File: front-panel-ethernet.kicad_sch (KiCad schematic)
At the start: 0 parts

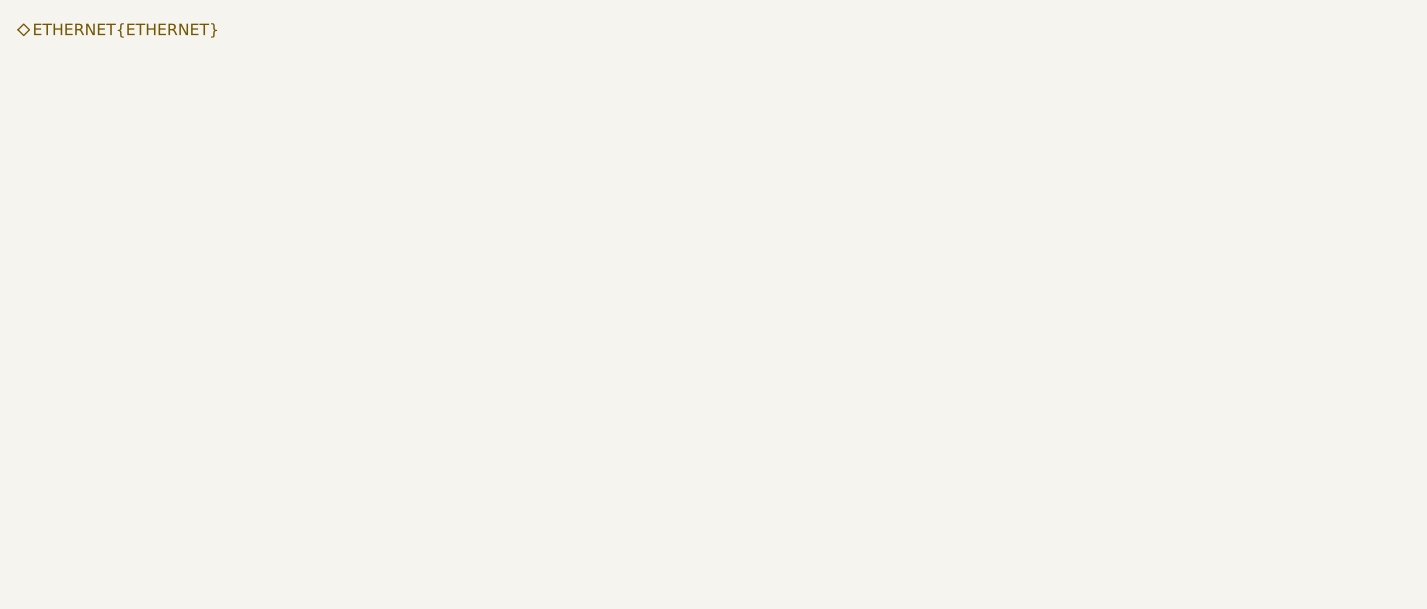
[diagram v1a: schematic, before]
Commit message: [#82153] Add RJ45 connector
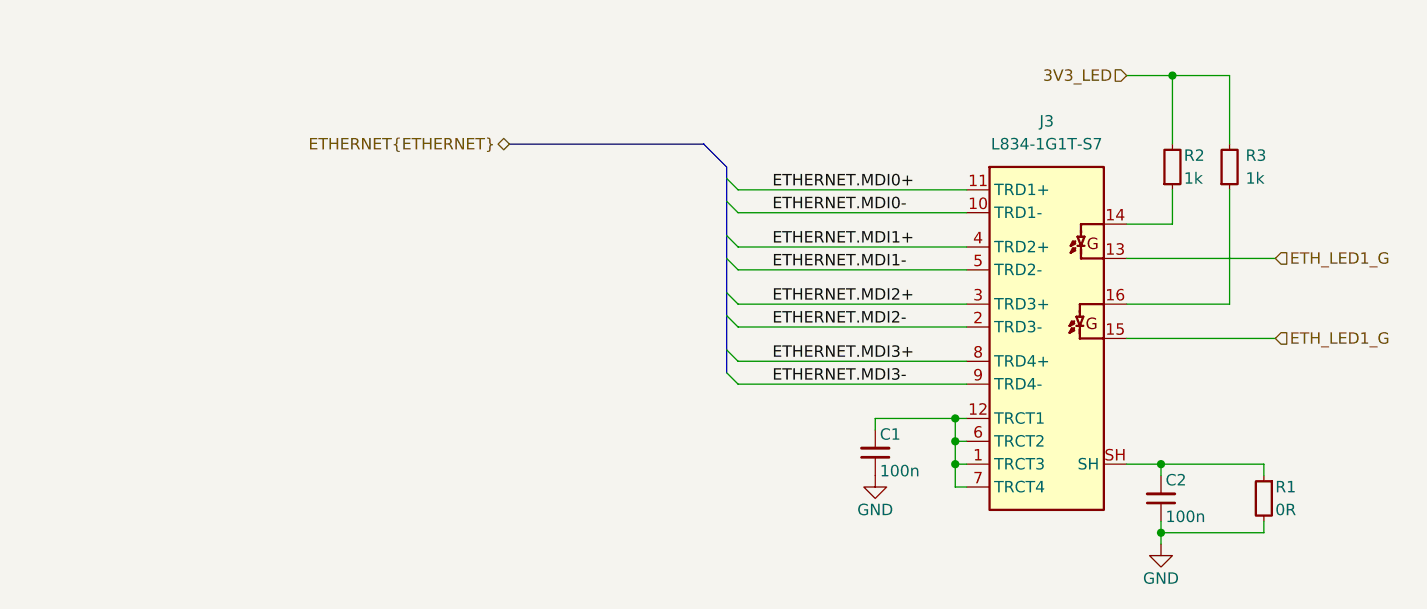
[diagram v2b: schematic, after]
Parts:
- added C1, C2: C_100n_0402, antmicro-footprints:C_0402_1005Metric, symbol antmicroCapacitors0402:C_100n_0402
- added J3: L834-1G1T-S7, antmicro-footprints:RJ45_BEL_L834-1G1T-S7, symbol antmicroModularConnectorsJacksWithMagnetics:L834-1G1T-S7
- added R1: R_0R_0402, antmicro-footprints:R_0402_1005Metric, symbol antmicroResistors0402:R_0R_0402
- added R2, R3: R_1k_0402, antmicro-footprints:R_0402_1005Metric, symbol antmicroResistors0402:R_1k_0402
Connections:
- new net: C2.2, J3.SH, R1.1
- new net: J3.14, R2.1
- new net: C1.2, J3.1 (TRCT3), J3.12 (TRCT1), J3.6 (TRCT2), J3.7 (TRCT4)
- new net: J3.16, R3.1
- new net 3V3_LED: R2.2, R3.2
- new net ETHERNET.MDI0+: J3.11 (TRD1+)
- new net ETHERNET.MDI0-: J3.10 (TRD1-)
- new net ETHERNET.MDI1+: J3.4 (TRD2+)
- new net ETHERNET.MDI1-: J3.5 (TRD2-)
- new net ETHERNET.MDI2+: J3.3 (TRD3+)
- new net ETHERNET.MDI2-: J3.2 (TRD3-)
- new net ETHERNET.MDI3+: J3.8 (TRD4+)
- new net ETHERNET.MDI3-: J3.9 (TRD4-)
- new net ETH_LED1_G: J3.13, J3.15
- new net GND: C1.1, C2.1, R1.2
